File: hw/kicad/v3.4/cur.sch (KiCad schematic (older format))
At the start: 2 parts

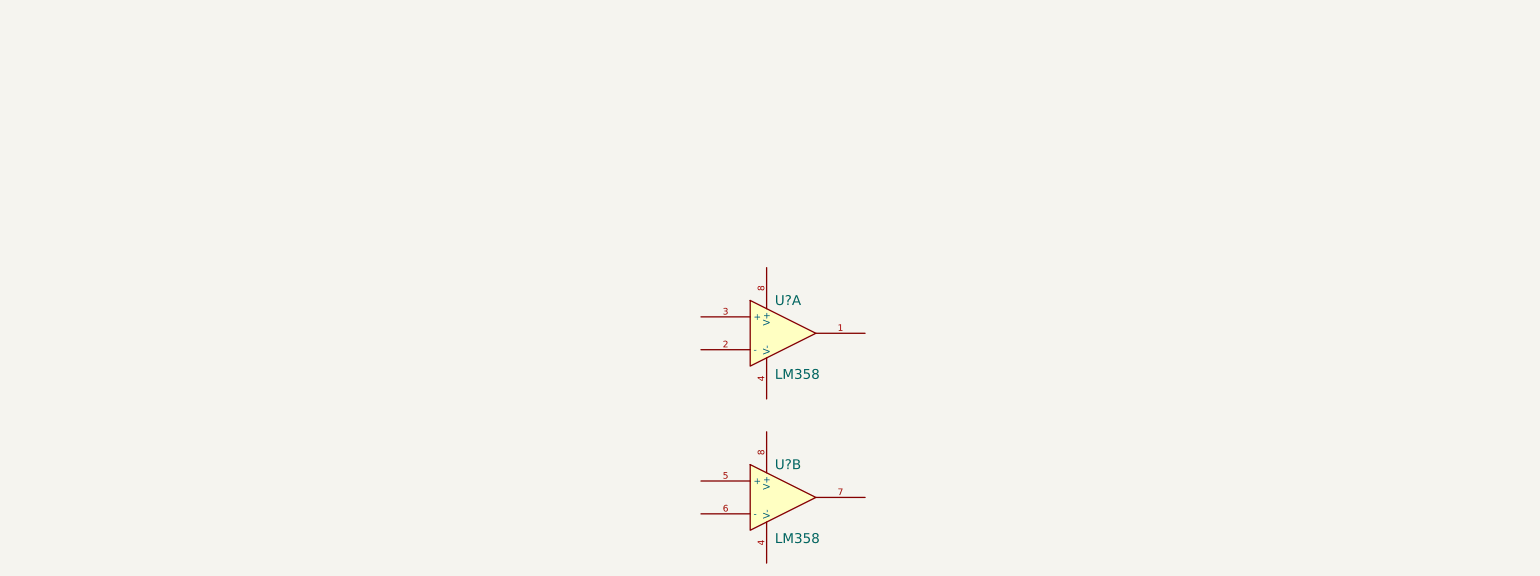
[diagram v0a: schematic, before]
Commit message: +cur sense, f4 pin remap
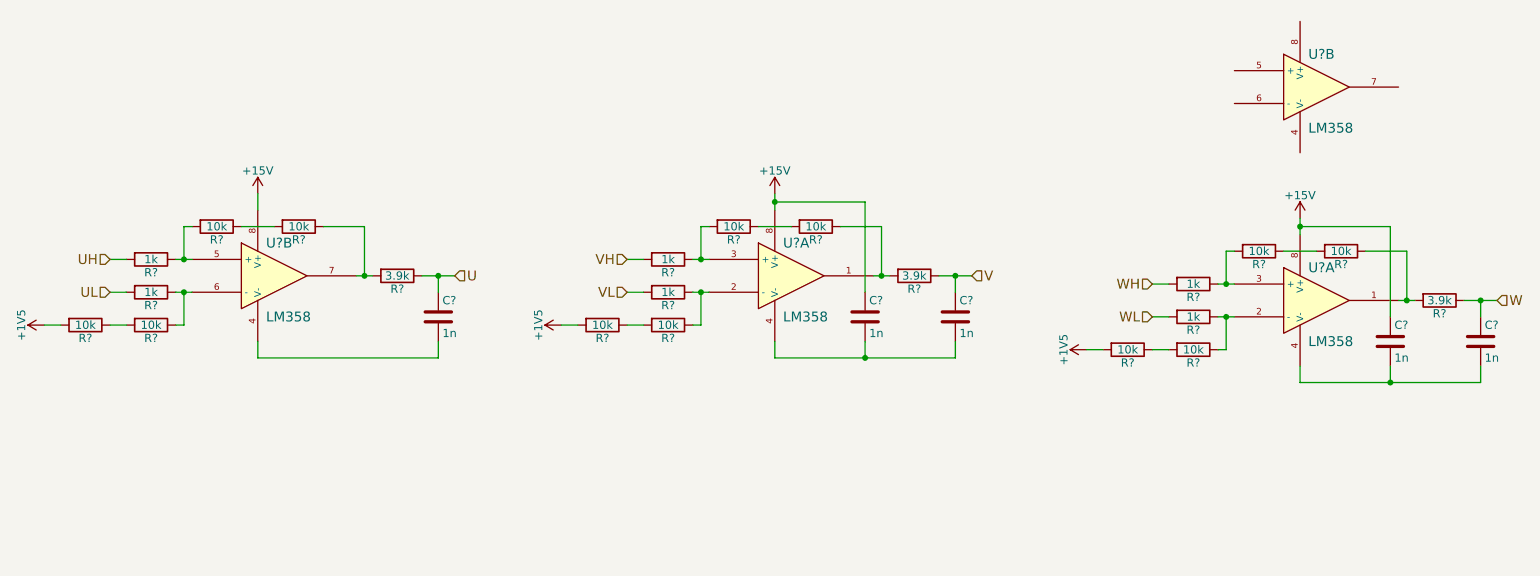
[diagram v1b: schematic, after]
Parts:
- added C? (x5): 1n, symbol C
- added R? (x6): 1k, symbol R
- added R? (x12): 10k, symbol R
- added R? (x3): 3.9k, symbol R
- added U? (x2): LM358, symbol LM358
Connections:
- net at U?.1: now also R?.1, R?.2
- net at U?.2 (-): now also R?.1, R?.1
- net at U?.3 (+): now also R?.1, R?.2
- net at U?.4 (V-): now also C?.2, C?.2
- net +15V: now reaches U?.8 (V+)
- net +15V: now also U?.8 (V+), C?.1, C?.1, U?.8 (V+)
- net at U?.4 (V-): now also C?.2
- net at U?.5 (+): now also R?.1, R?.2
- net at U?.6 (-): now also R?.1, R?.1
- net at U?.7: now also R?.1, R?.2
- new net: R?.1, R?.2 (x6)
- new net: R?.1, R?.1, U?.2 (-)
- new net: R?.1, R?.2, U?.3 (+)
- new net: R?.1, R?.2, U?.1
- new net: C?.2, C?.2, U?.4 (V-)
- new net +1V5: R?.2, R?.2, R?.2
- new net U: C?.1, R?.1
- new net UH: R?.2
- new net UL: R?.2
- new net V: C?.1, R?.1
- new net VH: R?.2
- new net VL: R?.2
- new net W: C?.1, R?.1
- new net WH: R?.2
- new net WL: R?.2
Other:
- moved on the sheet: U?A, U?B

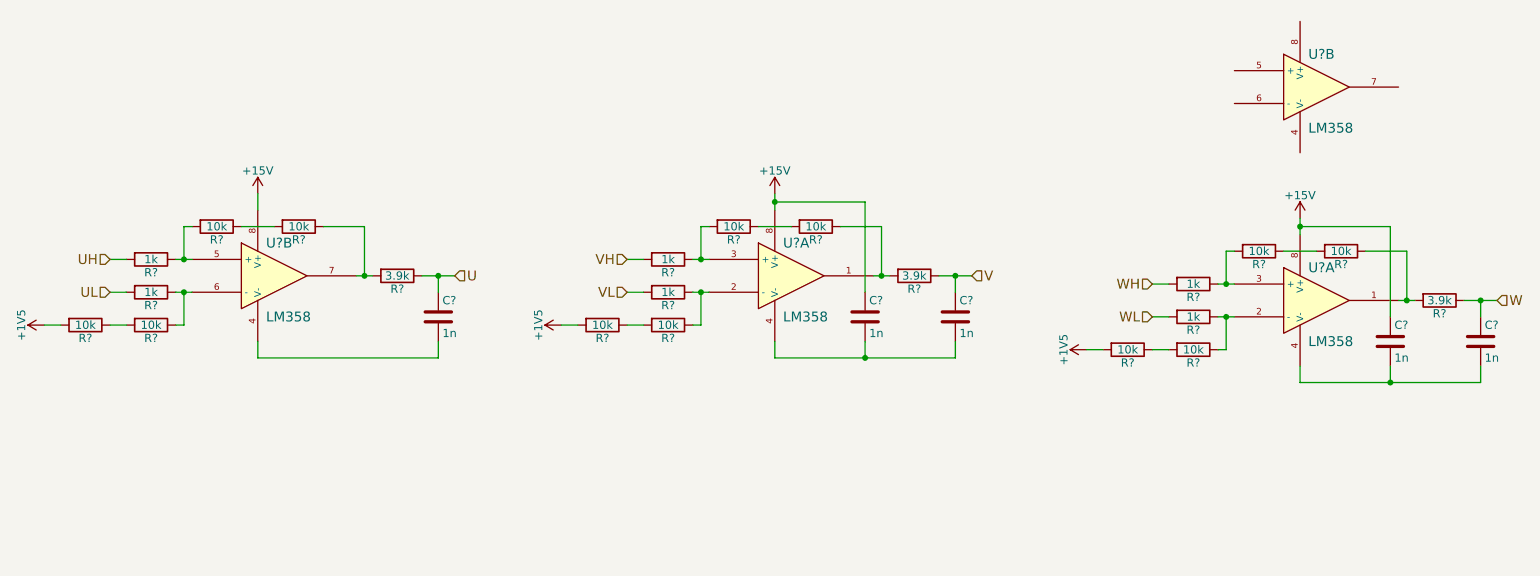
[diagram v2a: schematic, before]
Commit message: +f1 3.3V, viper fix
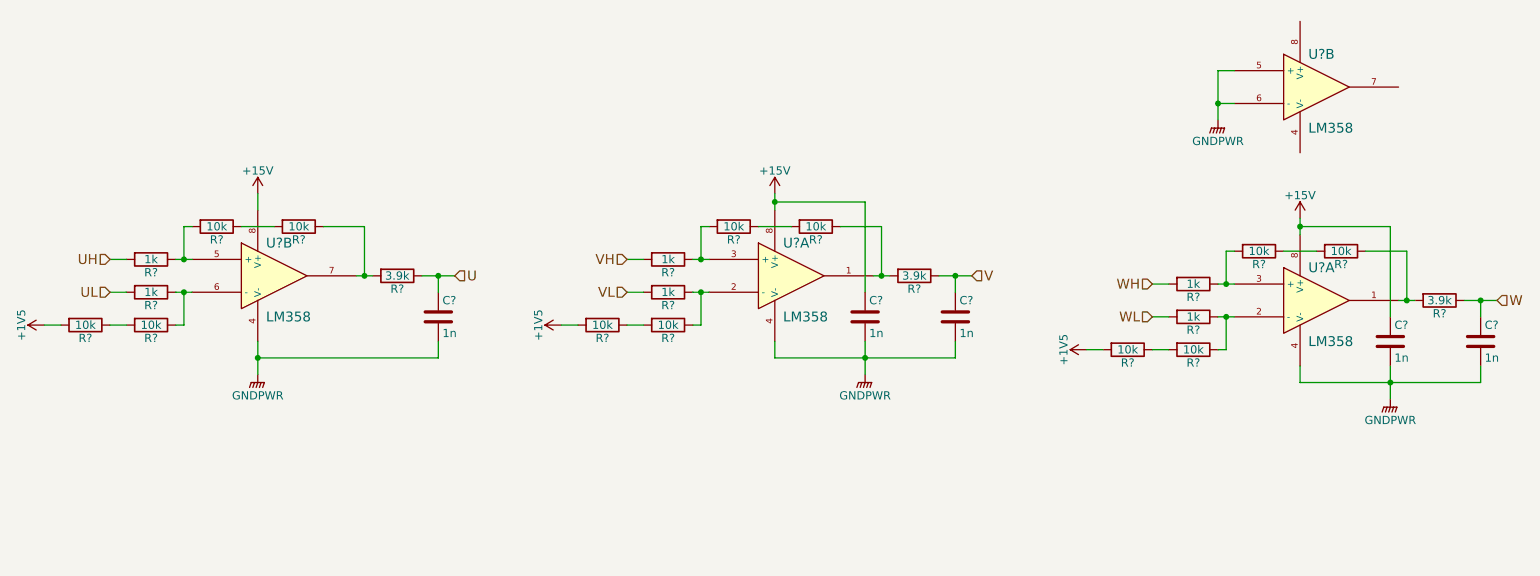
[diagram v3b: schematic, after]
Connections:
- net GNDPWR: now reaches C?.2, C?.2, U?.4 (V-)
- net GNDPWR: now also C?.2, C?.2, C?.2, U?.4 (V-), U?.4 (V-), U?.5 (+), U?.6 (-)
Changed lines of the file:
@@
 $EndComp
 Wire Wire Line
-	6500 2950 6500 2850
+	6500 2850 6500 3050
 Connection ~ 6500 2950
 Wire Wire Line
@@
 $EndComp
 Wire Wire Line
-	9700 3100 9700 3000
+	9700 3000 9700 3200
 Connection ~ 9700 3100
 Wire Wire Line
@@
 	3900 2950 2800 2950
 Wire Wire Line
-	2800 2950 2800 2850
+	2800 2850 2800 3050
 Wire Wire Line
 	2300 2750 2350 2750
@@
 	1    0    0    -1
 $EndComp
+$Comp
+L GNDPWR #PWR?
+U 1 1 566D0C9A
+P 9700 3200
+F 0 "#PWR?" H 9700 3000 50  0001 C CNN
+F 1 "GNDPWR" H 9700 3070 50  0000 C CNN
+F 2 "" H 9700 3150 60  0000 C CNN
+F 3 "" H 9700 3150 60  0000 C CNN
+	1    9700 3200
+	1    0    0    -1
+$EndComp
+$Comp
+L GNDPWR #PWR?
+U 1 1 566D0E0E
+P 6500 3050
+F 0 "#PWR?" H 6500 2850 50  0001 C CNN
+F 1 "GNDPWR" H 6500 2920 50  0000 C CNN
+F 2 "" H 6500 3000 60  0000 C CNN
+F 3 "" H 6500 3000 60  0000 C CNN
+	1    6500 3050
+	1    0    0    -1
+$EndComp
+$Comp
+L GNDPWR #PWR?
+U 1 1 566D0F5D
+P 2800 3050
+F 0 "#PWR?" H 2800 2850 50  0001 C CNN
+F 1 "GNDPWR" H 2800 2920 50  0000 C CNN
+F 2 "" H 2800 3000 60  0000 C CNN
+F 3 "" H 2800 3000 60  0000 C CNN
+	1    2800 3050
+	1    0    0    -1
+$EndComp
+Connection ~ 2800 2950
+$Comp
+L GNDPWR #PWR?
+U 1 1 566D1090
+P 8650 1500
+F 0 "#PWR?" H 8650 1300 50  0001 C CNN
+F 1 "GNDPWR" H 8650 1370 50  0000 C CNN
+F 2 "" H 8650 1450 60  0000 C CNN
+F 3 "" H 8650 1450 60  0000 C CNN
+	1    8650 1500
+	1    0    0    -1
+$EndComp
+Wire Wire Line
+	8750 1200 8650 1200
+Wire Wire Line
+	8650 1200 8650 1500
+Wire Wire Line
+	8750 1400 8650 1400
+Connection ~ 8650 1400
 $EndSCHEMATC

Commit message: hw v3.4
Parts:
- removed C?: 1n, symbol C
- removed R? (x6): 10k, symbol R
- added C?: 1n, symbol C
- added C?: 100n, symbol C
- added R? (x2): 200, symbol R
- C? (x2): value 1n -> 100n
- R? (x3): value 3.9k -> 1k
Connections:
- net +1V5: now also R?.2, R?.2, R?.2, C?.1, R?.1, R?.2
- net GNDPWR: now also U?.2 (-), U?.3 (+), C?.2, C?.2, R?.2; no longer U?.5 (+), U?.6 (-)
- net V: now also C?.1
- net at R?.1: now also R?.2, U?.1 (x3)
- net at R?.1, R?.1: now also U?.2 (-); no longer U?.6 (-)
- net at R?.1, R?.2: now also U?.3 (+); no longer U?.5 (+)
- new net +3.3VP: R?.1
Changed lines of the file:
@@
 EESchema Schematic File Version 2
 LIBS:conn
+LIBS:power
 LIBS:stmbl_3.4-cache
 EELAYER 25 0
@@
 $Comp
 L LM358 U?
-U 2 1 56697D11
+U 1 1 56697D11
 P 2900 2450
 F 0 "U?" H 2850 2650 60  0000 L CNN
@@
 F 2 "" H 2900 2450 60  0000 C CNN
 F 3 "" H 2900 2450 60  0000 C CNN
-	2    2900 2450
+	1    2900 2450
 	1    0    0    -1
 $EndComp
@@
 P 6800 2450
 F 0 "R?" V 6880 2450 50  0000 C CNN
-F 1 "3.9k" V 6800 2450 50  0000 C CNN
+F 1 "1k" V 6800 2450 50  0000 C CNN
 F 2 "" V 6730 2450 30  0000 C CNN
 F 3 "" H 6800 2450 30  0000 C CNN
@@
 $Comp
 L C C?
-U 1 1 56690E6B
+U 1 1 566DECB2
 P 7050 2700
 F 0 "C?" H 7075 2800 50  0000 L CNN
@@
 L +1V5 #PWR?
 U 1 1 56691046
-P 4650 2750
-F 0 "#PWR?" H 4650 2600 50  0001 C CNN
-F 1 "+1V5" H 4650 2890 50  0000 C CNN
-F 2 "" H 4650 2750 50  0000 C CNN
-F 3 "" H 4650 2750 50  0000 C CNN
-	1    4650 2750
+P 5050 2750
+F 0 "#PWR?" H 5050 2600 50  0001 C CNN
+F 1 "+1V5" H 5050 2890 50  0000 C CNN
+F 2 "" H 5050 2750 50  0000 C CNN
+F 3 "" H 5050 2750 50  0000 C CNN
+	1    5050 2750
 	0    -1   -1   0
 $EndComp
@@
 Wire Wire Line
 	5950 2050 5950 1950
-$Comp
-L R R?
-U 1 1 5669130A
-P 6200 2150
-F 0 "R?" V 6280 2150 50  0000 C CNN
-F 1 "10k" V 6200 2150 50  0000 C CNN
-F 2 "" V 6130 2150 30  0000 C CNN
-F 3 "" H 6200 2150 30  0000 C CNN
-	1    6200 2150
-	0    1    1    0
-$EndComp
-Wire Wire Line
-	6050 2150 5850 2150
-Wire Wire Line
-	6350 2150 6600 2150
+Wire Wire Line
+	5850 2150 6600 2150
 $Comp
 L R R?
@@
 	0    1    1    0
 $EndComp
-$Comp
-L R R?
-U 1 1 56691457
-P 4900 2750
-F 0 "R?" V 4980 2750 50  0000 C CNN
-F 1 "10k" V 4900 2750 50  0000 C CNN
-F 2 "" V 4830 2750 30  0000 C CNN
-F 3 "" H 4900 2750 30  0000 C CNN
-	1    4900 2750
-	0    1    1    0
-$EndComp
 Wire Wire Line
 	5050 2750 5150 2750
-Wire Wire Line
-	4650 2750 4750 2750
 $Comp
 L C C?
@@
 P 6500 2700
 F 0 "C?" H 6525 2800 50  0000 L CNN
-F 1 "1n" H 6525 2600 50  0000 L CNN
+F 1 "100n" H 6525 2600 50  0000 L CNN
 F 2 "" H 6538 2550 30  0000 C CNN
 F 3 "" H 6500 2700 60  0000 C CNN
@@
 P 10000 2600
 F 0 "R?" V 10080 2600 50  0000 C CNN
-F 1 "3.9k" V 10000 2600 50  0000 C CNN
+F 1 "1k" V 10000 2600 50  0000 C CNN
 F 2 "" V 9930 2600 30  0000 C CNN
 F 3 "" H 10000 2600 30  0000 C CNN
@@
 L +1V5 #PWR?
 U 1 1 56691AC8
-P 7850 2900
-F 0 "#PWR?" H 7850 2750 50  0001 C CNN
-F 1 "+1V5" H 7850 3040 50  0000 C CNN
-F 2 "" H 7850 2900 50  0000 C CNN
-F 3 "" H 7850 2900 50  0000 C CNN
-	1    7850 2900
+P 8250 2900
+F 0 "#PWR?" H 8250 2750 50  0001 C CNN
+F 1 "+1V5" H 8250 3040 50  0000 C CNN
+F 2 "" H 8250 2900 50  0000 C CNN
+F 3 "" H 8250 2900 50  0000 C CNN
+	1    8250 2900
 	0    -1   -1   0
 $EndComp
@@
 Wire Wire Line
 	9150 2200 9150 2100
-$Comp
-L R R?
-U 1 1 56691AD5
-P 9400 2300
-F 0 "R?" V 9480 2300 50  0000 C CNN
-F 1 "10k" V 9400 2300 50  0000 C CNN
-F 2 "" V 9330 2300 30  0000 C CNN
-F 3 "" H 9400 2300 30  0000 C CNN
-	1    9400 2300
-	0    1    1    0
-$EndComp
-Wire Wire Line
-	9250 2300 9050 2300
-Wire Wire Line
-	9550 2300 9800 2300
+Wire Wire Line
+	9050 2300 9800 2300
 $Comp
 L R R?
@@
 	0    1    1    0
 $EndComp
-$Comp
-L R R?
-U 1 1 56691AE3
-P 8100 2900
-F 0 "R?" V 8180 2900 50  0000 C CNN
-F 1 "10k" V 8100 2900 50  0000 C CNN
-F 2 "" V 8030 2900 30  0000 C CNN
-F 3 "" H 8100 2900 30  0000 C CNN
-	1    8100 2900
-	0    1    1    0
-$EndComp
 Wire Wire Line
 	8250 2900 8350 2900
-Wire Wire Line
-	7850 2900 7950 2900
 $Comp
 L C C?
@@
 P 9700 2850
 F 0 "C?" H 9725 2950 50  0000 L CNN
-F 1 "1n" H 9725 2750 50  0000 L CNN
+F 1 "100n" H 9725 2750 50  0000 L CNN
 F 2 "" H 9738 2700 30  0000 C CNN
 F 3 "" H 9700 2850 60  0000 C CNN
@@
 P 3650 2450
 F 0 "R?" V 3730 2450 50  0000 C CNN
-F 1 "3.9k" V 3650 2450 50  0000 C CNN
+F 1 "1k" V 3650 2450 50  0000 C CNN
 F 2 "" V 3580 2450 30  0000 C CNN
 F 3 "" H 3650 2450 30  0000 C CNN
@@
 L +1V5 #PWR?
 U 1 1 56691D4E
-P 1500 2750
-F 0 "#PWR?" H 1500 2600 50  0001 C CNN
-F 1 "+1V5" H 1500 2890 50  0000 C CNN
-F 2 "" H 1500 2750 50  0000 C CNN
-F 3 "" H 1500 2750 50  0000 C CNN
-	1    1500 2750
+P 1900 2750
+F 0 "#PWR?" H 1900 2600 50  0001 C CNN
+F 1 "+1V5" H 1900 2890 50  0000 C CNN
+F 2 "" H 1900 2750 50  0000 C CNN
+F 3 "" H 1900 2750 50  0000 C CNN
+	1    1900 2750
 	0    -1   -1   0
 $EndComp
@@
 Wire Wire Line
 	2800 2050 2800 1950
-$Comp
-L R R?
-U 1 1 56691D5B
-P 3050 2150
-F 0 "R?" V 3130 2150 50  0000 C CNN
-F 1 "10k" V 3050 2150 50  0000 C CNN
-F 2 "" V 2980 2150 30  0000 C CNN
-F 3 "" H 3050 2150 30  0000 C CNN
-	1    3050 2150
-	0    1    1    0
-$EndComp
-Wire Wire Line
-	2900 2150 2700 2150
-Wire Wire Line
-	3200 2150 3450 2150
+Wire Wire Line
+	2700 2150 3450 2150
 $Comp
 L R R?
@@
 	0    1    1    0
 $EndComp
-$Comp
-L R R?
-U 1 1 56691D69
-P 1750 2750
-F 0 "R?" V 1830 2750 50  0000 C CNN
-F 1 "10k" V 1750 2750 50  0000 C CNN
-F 2 "" V 1680 2750 30  0000 C CNN
-F 3 "" H 1750 2750 30  0000 C CNN
-	1    1750 2750
-	0    1    1    0
-$EndComp
-Wire Wire Line
-	1900 2750 2000 2750
-Wire Wire Line
-	1500 2750 1600 2750
 Text HLabel 1900 2350 0    60   Input ~ 0
 UH
@@
 $Comp
 L LM358 U?
-U 2 1 566922D2
+U 1 1 566922D2
 P 9250 1300
 F 0 "U?" H 9200 1500 60  0000 L CNN
@@
 F 2 "" H 9250 1300 60  0000 C CNN
 F 3 "" H 9250 1300 60  0000 C CNN
-	2    9250 1300
+	1    9250 1300
 	1    0    0    -1
 $EndComp
@@
 	8750 1400 8650 1400
 Connection ~ 8650 1400
+Wire Wire Line
+	1900 2750 2000 2750
+$Comp
+L R R?
+U 1 1 568321D2
+P 4300 1250
+F 0 "R?" V 4380 1250 50  0000 C CNN
+F 1 "200" V 4300 1250 50  0000 C CNN
+F 2 "" V 4230 1250 30  0000 C CNN
+F 3 "" H 4300 1250 30  0000 C CNN
+	1    4300 1250
+	1    0    0    -1
+$EndComp
+$Comp
+L +3.3VP #PWR?
+U 1 1 5683229B
+P 4300 1000
+F 0 "#PWR?" H 4450 950 50  0001 C CNN
+F 1 "+3.3VP" H 4300 1100 50  0000 C CNN
+F 2 "" H 4300 1000 60  0000 C CNN
+F 3 "" H 4300 1000 60  0000 C CNN
+	1    4300 1000
+	1    0    0    -1
+$EndComp
+$Comp
+L GNDPWR #PWR?
+U 1 1 568322FA
+P 4300 2100
+F 0 "#PWR?" H 4300 1900 50  0001 C CNN
+F 1 "GNDPWR" H 4300 1970 50  0000 C CNN
+F 2 "" H 4300 2050 60  0000 C CNN
+F 3 "" H 4300 2050 60  0000 C CNN
+	1    4300 2100
+	1    0    0    -1
+$EndComp
+$Comp
+L R R?
+U 1 1 56832370
+P 4300 1750
+F 0 "R?" V 4380 1750 50  0000 C CNN
+F 1 "200" V 4300 1750 50  0000 C CNN
+F 2 "" V 4230 1750 30  0000 C CNN
+F 3 "" H 4300 1750 30  0000 C CNN
+	1    4300 1750
+	1    0    0    -1
+$EndComp
+Wire Wire Line
+	4300 1900 4300 2100
+Wire Wire Line
+	4300 1600 4300 1400
+Wire Wire Line
+	4300 1100 4300 1000
+Wire Wire Line
+	4600 1500 4300 1500
+Wire Wire Line
+	4600 1300 4600 1600
+Connection ~ 4300 1500
+$Comp
+L +1V5 #PWR?
+U 1 1 56833E7F
+P 4600 1300
+F 0 "#PWR?" H 4600 1150 50  0001 C CNN
+F 1 "+1V5" H 4600 1440 50  0000 C CNN
+F 2 "" H 4600 1300 50  0000 C CNN
+F 3 "" H 4600 1300 50  0000 C CNN
+	1    4600 1300
+	1    0    0    -1
+$EndComp
+$Comp
+L C C?
+U 1 1 56834179
+P 4600 1750
+F 0 "C?" H 4625 1850 50  0000 L CNN
+F 1 "100n" H 4625 1650 50  0000 L CNN
+F 2 "" H 4638 1600 30  0000 C CNN
+F 3 "" H 4600 1750 60  0000 C CNN
+	1    4600 1750
+	1    0    0    -1
+$EndComp
+Wire Wire Line
+	4300 2000 4600 2000
+Wire Wire Line
+	4600 2000 4600 1900
+Connection ~ 4300 2000
+Connection ~ 4600 1500
 $EndSCHEMATC

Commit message: hw v3.4 +testpoints
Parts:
- added T? (x4): testpoint, symbol testpoint
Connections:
- net +1V5: now also T?.1
- net U: now also T?.1
- net V: now also T?.1
- net W: now also T?.1
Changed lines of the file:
@@
 EESchema Schematic File Version 2
-LIBS:conn
 LIBS:power
 LIBS:stmbl_3.4-cache
@@
 	6950 2450 7150 2450
 Wire Wire Line
-	7050 2450 7050 2550
+	7050 2350 7050 2550
 Wire Wire Line
 	7050 2850 7050 2950
@@
 	10150 2600 10350 2600
 Wire Wire Line
-	10250 2600 10250 2700
+	10250 2500 10250 2700
 Wire Wire Line
 	10250 3000 10250 3100
@@
 	3800 2450 4000 2450
 Wire Wire Line
-	3900 2450 3900 2550
+	3900 2350 3900 2550
 Wire Wire Line
 	3900 2850 3900 2950
@@
 	4300 1100 4300 1000
 Wire Wire Line
-	4600 1500 4300 1500
+	4300 1500 4700 1500
 Wire Wire Line
 	4600 1300 4600 1600
@@
 Connection ~ 4300 2000
 Connection ~ 4600 1500
+$Comp
+L testpoint T?
+U 1 1 56823817
+P 3900 2150
+F 0 "T?" H 3900 2250 60  0000 C CNN
+F 1 "testpoint" H 3900 2050 60  0000 C CNN
+F 2 "" H 3900 2150 60  0000 C CNN
+F 3 "" H 3900 2150 60  0000 C CNN
+	1    3900 2150
+	0    -1   -1   0
+$EndComp
+$Comp
+L testpoint T?
+U 1 1 568238DC
+P 7050 2150
+F 0 "T?" H 7050 2250 60  0000 C CNN
+F 1 "testpoint" H 7050 2050 60  0000 C CNN
+F 2 "" H 7050 2150 60  0000 C CNN
+F 3 "" H 7050 2150 60  0000 C CNN
+	1    7050 2150
+	0    -1   -1   0
+$EndComp
+$Comp
+L testpoint T?
+U 1 1 56823B0A
+P 4900 1500
+F 0 "T?" H 4900 1600 60  0000 C CNN
+F 1 "testpoint" H 4900 1400 60  0000 C CNN
+F 2 "" H 4900 1500 60  0000 C CNN
+F 3 "" H 4900 1500 60  0000 C CNN
+	1    4900 1500
+	1    0    0    -1
+$EndComp
+$Comp
+L testpoint T?
+U 1 1 56823DB5
+P 10250 2300
+F 0 "T?" H 10250 2400 60  0000 C CNN
+F 1 "testpoint" H 10250 2200 60  0000 C CNN
+F 2 "" H 10250 2300 60  0000 C CNN
+F 3 "" H 10250 2300 60  0000 C CNN
+	1    10250 2300
+	0    -1   -1   0
+$EndComp
 $EndSCHEMATC
